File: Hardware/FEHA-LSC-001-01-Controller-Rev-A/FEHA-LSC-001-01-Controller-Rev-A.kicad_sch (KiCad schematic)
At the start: 40 parts, among them CN1 HDGC4001SMD-S-2P, CN2 HDGC4001SMD-S-2P, CN3 USB_DEBUG, Q1 HL2310A, Q2 SI2356DS-T1-GE3, U1 TPS560430XFDBVR, U2 ESP32-C3-MINI-1-H4X(4MB)

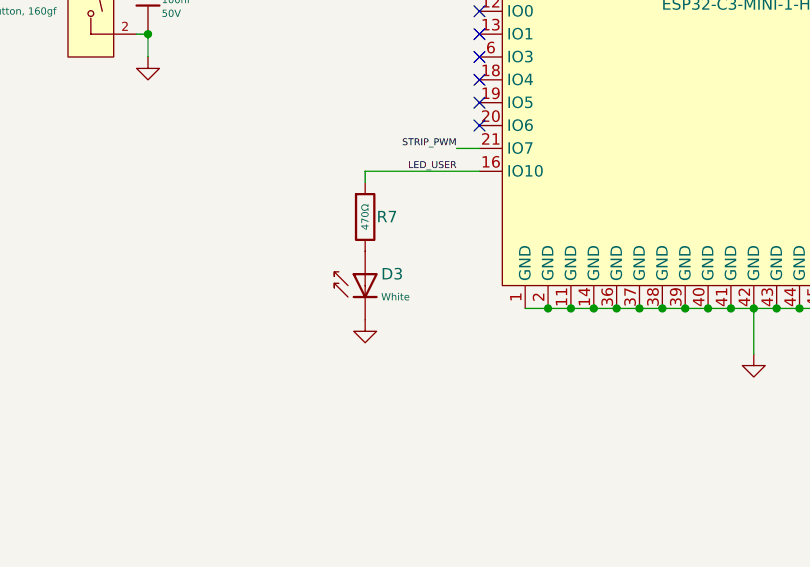
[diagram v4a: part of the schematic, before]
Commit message: LSC: yellow status LED (DEC-28); §10 bring-up plan (review TEST-3)
D3 changed to KT-0805Y (C2296): off in normal operation, setup and fault
by blink pattern; ~2 V Vf lets the 470 ohm R7 set the current. House
sourcing fields restored after Change Symbol. Netlist otherwise
unchanged; ERC 0 errors.

Spec §10: test-point plan and five-step bring-up order (USB first, then
current-limited 24 V). Review TEST-3 closed, PART-5 round 2 recorded.

Co-Authored-By: Claude Opus 5.5 <noreply@anthropic.com>
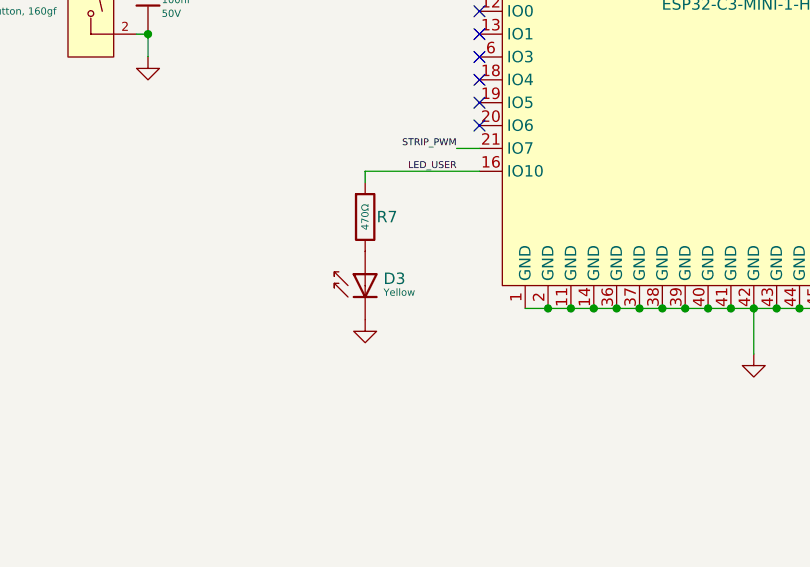
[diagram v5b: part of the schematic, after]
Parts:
- removed D3: White, PCM_JLCPCB:D_0805, symbol PCM_JLCPCB-Diodes:LED,0805,White
- added D3: Yellow, PCM_JLCPCB:D_0805, symbol PCM_JLCPCB-Diodes:LED,0805,Yellow
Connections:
- net GND: now also D3.1
- net at R7.2: now also D3.2
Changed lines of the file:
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@@
 	)
 	(symbol
+		(lib_id "PCM_JLCPCB-Diodes:LED,0805,Yellow")
+		(at 172.72 107.95 0)
+		(unit 1)
+		(body_style 1)
+		(exclude_from_sim no)
+		(in_bom yes)
+		(on_board yes)
+		(in_pos_files yes)
+		(dnp no)
+		(property "Reference" "D3"
+			(at 174.752 107.188 0)
+			(show_name no)
+			(do_not_autoplace no)
+			(effects
+				(font
+					(size 1.27 1.27)
+				)
+				(justify left)
+			)
+		)
+		(property "Value" "Yellow"
+			(at 174.752 108.712 0)
+			(show_name no)
+			(do_not_autoplace no)
+			(effects
+				(font
+					(size 0.8 0.8)
+				)
+				(justify left)
+			)
+		)
+		(property "Footprint" "PCM_JLCPCB:D_0805"
+			(at 170.942 107.95 90)
+			(hide yes)
+			(show_name no)
+			(do_not_autoplace no)
+			(effects
+				(font
+					(size 1.27 1.27)
+				)
+			)
+		)
+		(property "Datasheet" "https://www.lcsc.com/datasheet/lcsc_datasheet_1806151129_Hubei-KENTO-Elec-KT-0805Y_C2296.pdf"
+			(at 172.72 107.95 0)
+			(hide yes)
+			(show_name no)
+			(do_not_autoplace no)
+			(effects
+				(font
+					(size 1.27 1.27)
+				)
+			)
+		)
+		(property "Description" "Yellow 0805 LED Indication - Discrete ROHS"
+			(at 172.72 107.95 0)
+			(hide yes)
+			(show_name no)
+			(do_not_autoplace no)
+			(effects
+				(font
+					(size 1.27 1.27)
+				)
+			)
+		)
+		(property "LCSC" "C2296"
+			(at 172.72 107.95 0)
+			(hide yes)
+			(show_name no)
+			(do_not_autoplace no)
+			(effects
+				(font
+					(size 1.27 1.27)
+				)
+			)
+		)
+		(property "Stock" "662678"
+			(at 172.72 107.95 0)
+			(hide yes)
+			(show_name no)
+			(do_not_autoplace no)
+			(effects
+				(font
+					(size 1.27 1.27)
+				)
+			)
+		)
+		(property "Price" "0.015USD"
+			(at 172.72 107.95 0)
+			(hide yes)
+			(show_name no)
+			(do_not_autoplace no)
+			(effects
+				(font
+					(size 1.27 1.27)
+				)
+			)
+		)
+		(property "Process" "SMT"
+			(at 172.72 107.95 0)
+			(hide yes)
+			(show_name no)
+			(do_not_autoplace no)
+			(effects
+				(font
+					(size 1.27 1.27)
+				)
+			)
+		)
+		(property "Minimum Qty" "20"
+			(at 172.72 107.95 0)
+			(hide yes)
+			(show_name no)
+			(do_not_autoplace no)
+			(effects
+				(font
+					(size 1.27 1.27)
+				)
+			)
+		)
+		(property "Attrition Qty" "10"
+			(at 172.72 107.95 0)
+			(hide yes)
+			(show_name no)
+			(do_not_autoplace no)
+			(effects
+				(font
+					(size 1.27 1.27)
+				)
+			)
+		)
+		(property "Class" "Basic Component"
+			(at 172.72 107.95 0)
+			(hide yes)
+			(show_name no)
+			(do_not_autoplace no)
+			(effects
+				(font
+					(size 1.27 1.27)
+				)
+			)
+		)
+		(property "Category" "Optocouplers & LEDs & Infrared,Light Emitting Diodes (LED)"
+			(at 172.72 107.95 0)
+			(hide yes)
+			(show_name no)
+			(do_not_autoplace no)
+			(effects
+				(font
+					(size 1.27 1.27)
+				)
+			)
+		)
+		(property "Manufacturer" "Hubei KENTO Elec"
+			(at 172.72 107.95 0)
+			(hide yes)
+			(show_name no)
+			(do_not_autoplace no)
+			(effects
+				(font
+					(size 1.27 1.27)
+				)
+			)
+		)
+		(property "Part" "KT-0805Y"
+			(at 172.72 107.95 0)
+			(hide yes)
+			(show_name no)
+			(do_not_autoplace no)
+			(effects
+				(font
+					(size 1.27 1.27)
+				)
+			)
+		)
+    (property "Mfr. Part #" "KT-0805Y" (at 172.72 107.95 0)
+      (effects (font (size 1.27 1.27)) (hide yes))
+    )
+    (property "LCSC Part #" "C2296" (at 172.72 107.95 0)
+      (effects (font (size 1.27 1.27)) (hide yes))
+    )
+    (property "Package" "0805" (at 172.72 107.95 0)
+      (effects (font (size 1.27 1.27)) (hide yes))
+    )
+		(pin "1"
+		)
+		(pin "2"
+		)
+		(instances
+			(project "FEHA-LSC-001-01-Controller-Rev-A"
+				(path "/b6e06938-22b9-4085-a332-ab512658a3b8"
+					(reference "D3")
+					(unit 1)
+				)
+			)
+		)
+	)
+	(symbol
 		(lib_id "_FEHA-LSC-001:TPS560430XFDBVR")
 		(at 67.31 99.06 0)
@@
 					(unit 1)
 				)
-			)
-		)
-	)
-	(symbol
-		(lib_id "PCM_JLCPCB-Diodes:LED,0805,White")
-		(at 172.72 107.95 0)
-		(unit 1)
-		(body_style 1)
-		(exclude_from_sim no)
-		(in_bom yes)
-		(on_board yes)
-		(in_pos_files yes)
-		(dnp no)
-		(property "Reference" "D3"
-			(at 174.498 106.6799 0)
-			(show_name no)
-			(do_not_autoplace no)
-			(effects
-				(font
-					(size 1.27 1.27)
-				)
-				(justify left)
-			)
-		)
-		(property "Value" "White"
-			(at 174.498 109.22 0)
-			(show_name no)
-			(do_not_autoplace no)
-			(effects
-				(font
-					(size 0.8 0.8)
-				)
-				(justify left)
-			)
-		)
-		(property "Footprint" "PCM_JLCPCB:D_0805"
-			(at 170.942 107.95 90)
-			(hide yes)
-			(show_name no)
-			(do_not_autoplace no)
-			(effects
-				(font
-					(size 1.27 1.27)
-				)
-			)
-		)
-		(property "Datasheet" "https://www.lcsc.com/datasheet/lcsc_datasheet_2305091500_Hubei-KENTO-Elec-KT-0805W_C34499.pdf"
-			(at 172.72 107.95 0)
-			(hide yes)
-			(show_name no)
-			(do_not_autoplace no)
-			(effects
-				(font
-					(size 1.27 1.27)
-				)
-			)
-		)
-		(property "Description" "0805 LED Indication - Discrete ROHS"
-			(at 172.72 107.95 0)
-			(hide yes)
-			(show_name no)
-			(do_not_autoplace no)
-			(effects
-				(font
-					(size 1.27 1.27)
-				)
-			)
-		)
-		(property "LCSC" "C34499"
-			(at 172.72 107.95 0)
-			(hide yes)
-			(show_name no)
-			(do_not_autoplace no)
-			(effects
-				(font
-					(size 1.27 1.27)
-				)
-			)
-		)
-		(property "Stock" "505726"
-			(at 172.72 107.95 0)
-			(hide yes)
-			(show_name no)
-			(do_not_autoplace no)
-			(effects
-				(font
-					(size 1.27 1.27)
-				)
-			)
-		)
-		(property "Price" "0.020USD"
-			(at 172.72 107.95 0)
-			(hide yes)
-			(show_name no)
-			(do_not_autoplace no)
-			(effects
-				(font
-					(size 1.27 1.27)
-				)
-			)
-		)
-		(property "Process" "SMT"
-			(at 172.72 107.95 0)
-			(hide yes)
-			(show_name no)
-			(do_not_autoplace no)
-			(effects
-				(font
-					(size 1.27 1.27)
-				)
-			)
-		)
-		(property "Minimum Qty" "20"
-			(at 172.72 107.95 0)
-			(hide yes)
-			(show_name no)
-			(do_not_autoplace no)
-			(effects
-				(font
-					(size 1.27 1.27)
-				)
-			)
-		)
-		(property "Attrition Qty" "8"
-			(at 172.72 107.95 0)
-			(hide yes)
-			(show_name no)
-			(do_not_autoplace no)
-			(effects
-				(font
-					(size 1.27 1.27)
-				)
-			)
-		)
-		(property "Class" "Basic Component"
-			(at 172.72 107.95 0)
-			(hide yes)
-			(show_name no)
-			(do_not_autoplace no)
-			(effects
-				(font
-					(size 1.27 1.27)
-				)
-			)
-		)
-		(property "Category" "Optocouplers & LEDs & Infrared,Light Emitting Diodes (LED)"
-			(at 172.72 107.95 0)
-			(hide yes)
-			(show_name no)
-			(do_not_autoplace no)
-			(effects
-				(font
-					(size 1.27 1.27)
-				)
-			)
-		)
-		(property "Manufacturer" "Hubei KENTO Elec"
-			(at 172.72 107.95 0)
-			(hide yes)
-			(show_name no)
-			(do_not_autoplace no)
-			(effects
-				(font
-					(size 1.27 1.27)
-				)
-			)
-		)
-		(property "Part" "KT-0805W"
-			(at 172.72 107.95 0)
-			(hide yes)
-			(show_name no)
-			(do_not_autoplace no)
-			(effects
-				(font
-					(size 1.27 1.27)
-				)
-			)
-		)
-		(property "Mfr. Part #" "KT-0805W"
-			(at 172.72 107.95 0)
-			(hide yes)
-			(show_name no)
-			(do_not_autoplace no)
-			(effects
-				(font
-					(size 1.27 1.27)
-				)
-			)
-		)
-		(property "LCSC Part #" "C34499"
-			(at 172.72 107.95 0)
-			(hide yes)
-			(show_name no)
-			(do_not_autoplace no)
-			(effects
-				(font
-					(size 1.27 1.27)
-				)
-			)
-		)
-		(property "Package" "0805"
-			(at 172.72 107.95 0)
-			(hide yes)
-			(show_name no)
-			(do_not_autoplace no)
-			(effects
-				(font
-					(size 1.27 1.27)
-				)
-			)
-		)
-		(property "Color" ""
-			(at 172.72 107.95 0)
-			(hide yes)
-			(show_name no)
-			(do_not_autoplace no)
-			(effects
-				(font
-					(size 1.27 1.27)
-				)
-			)
-		)
-		(property "Sim.Pins" ""
-			(at 172.72 107.95 0)
-			(hide yes)
-			(show_name no)
-			(do_not_autoplace no)
-			(effects
-				(font
-					(size 1.27 1.27)
-				)
-			)
-		)
-		(pin "2"
-		)
-		(pin "1"
-		)
-		(instances
-			(project "FEHA-LSC-001-01-Controller-Rev-A"
-				(path "/b6e06938-22b9-4085-a332-ab512658a3b8"
-					(reference "D3")
-					(unit 1)
-				)
